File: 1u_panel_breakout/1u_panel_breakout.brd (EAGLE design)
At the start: 33 x 32 mm, 6 parts

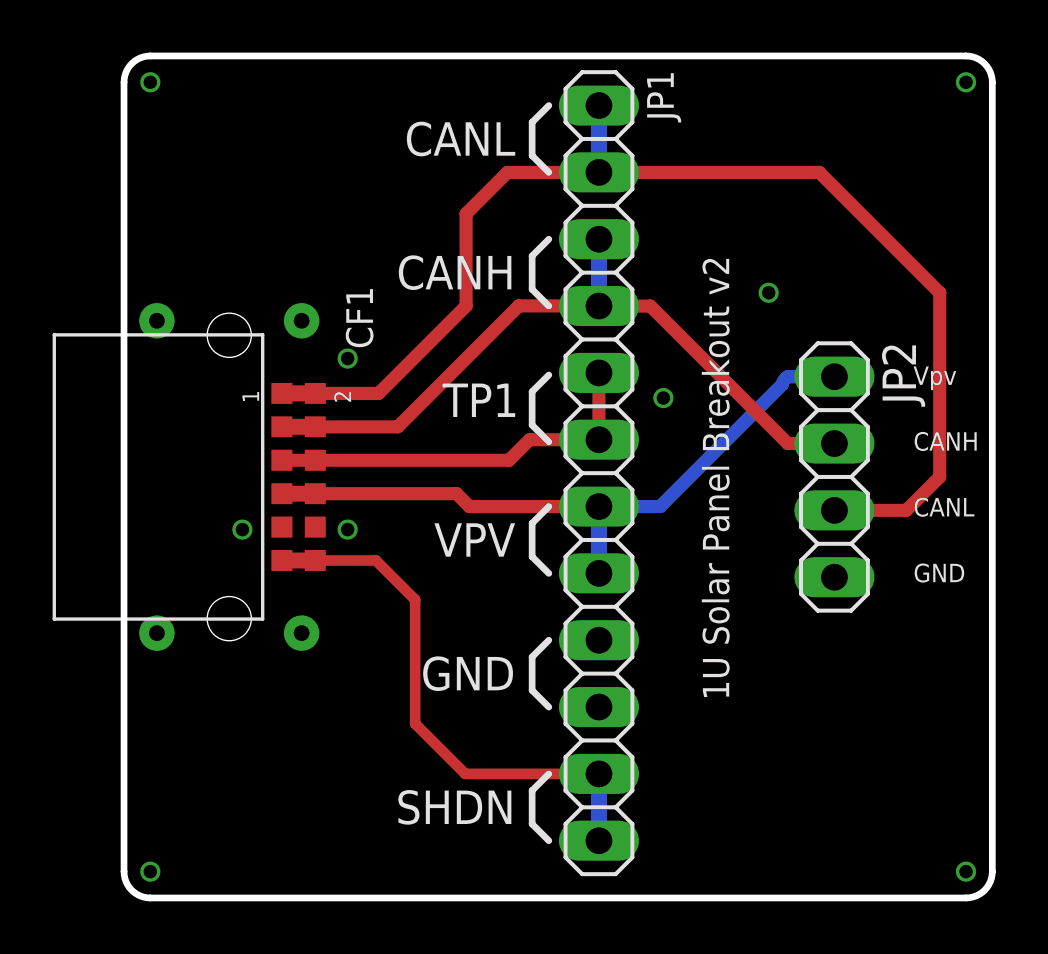
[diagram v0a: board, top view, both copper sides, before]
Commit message: Added part numbers to odd connectors.
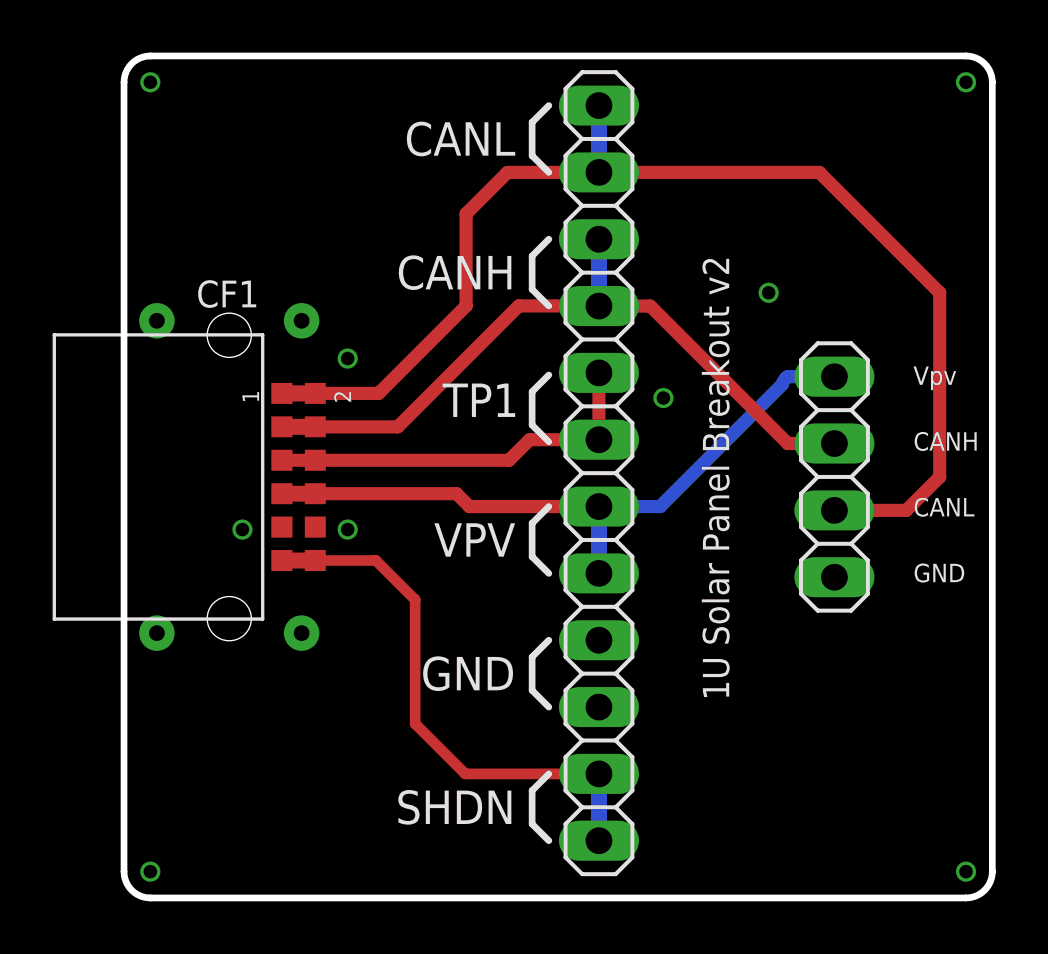
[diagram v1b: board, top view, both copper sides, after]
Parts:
- CF1: value ORESAT-SOLARPANEL-CARD-12PIN -> 15150122401000
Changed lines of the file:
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@@
 <layer number="14" name="Route14" color="1" fill="6" visible="no" active="no"/>
 <layer number="15" name="Route15" color="4" fill="6" visible="no" active="no"/>
-<layer number="16" name="Bottom" color="1" fill="1" visible="yes" active="yes"/>
+<layer number="16" name="Bottom" color="1" fill="1" visible="no" active="yes"/>
 <layer number="17" name="Pads" color="2" fill="1" visible="yes" active="yes"/>
 <layer number="18" name="Vias" color="2" fill="1" visible="yes" active="yes"/>
@@
 <layer number="20" name="Dimension" color="15" fill="1" visible="yes" active="yes"/>
 <layer number="21" name="tPlace" color="7" fill="1" visible="yes" active="yes"/>
-<layer number="22" name="bPlace" color="7" fill="1" visible="yes" active="yes"/>
+<layer number="22" name="bPlace" color="7" fill="1" visible="no" active="yes"/>
 <layer number="23" name="tOrigins" color="15" fill="1" visible="yes" active="yes"/>
-<layer number="24" name="bOrigins" color="15" fill="1" visible="yes" active="yes"/>
-<layer number="25" name="tNames" color="7" fill="1" visible="no" active="yes"/>
+<layer number="24" name="bOrigins" color="15" fill="1" visible="no" active="yes"/>
+<layer number="25" name="tNames" color="7" fill="1" visible="yes" active="yes"/>
 <layer number="26" name="bNames" color="7" fill="1" visible="no" active="yes"/>
 <layer number="27" name="tValues" color="7" fill="1" visible="no" active="yes"/>
 <layer number="28" name="bValues" color="7" fill="1" visible="no" active="yes"/>
 <layer number="29" name="tStop" color="7" fill="3" visible="yes" active="yes"/>
-<layer number="30" name="bStop" color="7" fill="6" visible="yes" active="yes"/>
+<layer number="30" name="bStop" color="7" fill="6" visible="no" active="yes"/>
 <layer number="31" name="tCream" color="7" fill="4" visible="no" active="yes"/>
 <layer number="32" name="bCream" color="7" fill="5" visible="no" active="yes"/>
@@
 <layer number="46" name="Milling" color="3" fill="1" visible="yes" active="yes"/>
 <layer number="47" name="Measures" color="7" fill="1" visible="no" active="yes"/>
-<layer number="48" name="Document" color="7" fill="1" visible="yes" active="yes"/>
-<layer number="49" name="Reference" color="7" fill="1" visible="yes" active="yes"/>
+<layer number="48" name="Document" color="7" fill="1" visible="no" active="yes"/>
+<layer number="49" name="Reference" color="7" fill="1" visible="no" active="yes"/>
 <layer number="50" name="dxf" color="7" fill="1" visible="no" active="no"/>
-<layer number="51" name="tDocu" color="7" fill="1" visible="yes" active="yes"/>
-<layer number="52" name="bDocu" color="7" fill="1" visible="yes" active="yes"/>
+<layer number="51" name="tDocu" color="7" fill="1" visible="no" active="yes"/>
+<layer number="52" name="bDocu" color="7" fill="1" visible="no" active="yes"/>
 <layer number="53" name="tGND_GNDA" color="7" fill="9" visible="no" active="no"/>
 <layer number="54" name="bGND_GNDA" color="1" fill="9" visible="no" active="no"/>
@@
 </autorouter>
 <elements>
-<element name="CF1" library="oresat-connectors" package="CON-1.27-M-RA-HARTING-1515012X401XXX" value="ORESAT-SOLARPANEL-CARD-12PIN" x="4" y="16" smashed="yes" rot="R270">
-<attribute name="NAME" x="8.445" y="23.255" size="1.016" layer="25" ratio="20" rot="R270"/>
+<element name="CF1" library="oresat-connectors" package="CON-1.27-M-RA-HARTING-1515012X401XXX" value="15150122401000" x="4" y="16" smashed="yes" rot="R270">
+<attribute name="NAME" x="2.745" y="22.445" size="1.016" layer="25" ratio="20"/>
 <attribute name="VALUE" x="-0.445" y="22.62" size="0.635" layer="27" ratio="20" rot="R270"/>
 </element>
 <element name="JP1" library="pinhead" package="1X12" value="" x="18.05" y="16.145" smashed="yes" rot="R270">
-<attribute name="NAME" x="19.8788" y="31.4612" size="1.016" layer="25" ratio="10" rot="R270"/>
 <attribute name="VALUE" x="14.875" y="31.385" size="1.27" layer="27" rot="R270"/>
 </element>
-<element name="JP2" library="pinhead" library_urn="urn:adsk.eagle:library:325" package="1X04" package3d_urn="urn:adsk.eagle:package:22407/2" value="" x="27" y="16" rot="R270"/>
+<element name="JP2" library="pinhead" library_urn="urn:adsk.eagle:library:325" package="1X04" package3d_urn="urn:adsk.eagle:package:22407/2" value="" x="27" y="16" smashed="yes" rot="R270">
+<attribute name="VALUE" x="23.825" y="21.08" size="1.27" layer="27" rot="R270"/>
+</element>
 <element name="U$1" library="oresat-misc" package="SCOPE_CLIP" value="SCOPE_CLIP" x="22.5" y="2" rot="R270"/>
 <element name="U$2" library="oresat-misc" package="SCOPE_CLIP" value="SCOPE_CLIP" x="22" y="30" rot="R90"/>

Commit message: Updated solar breakout board (for main connector).
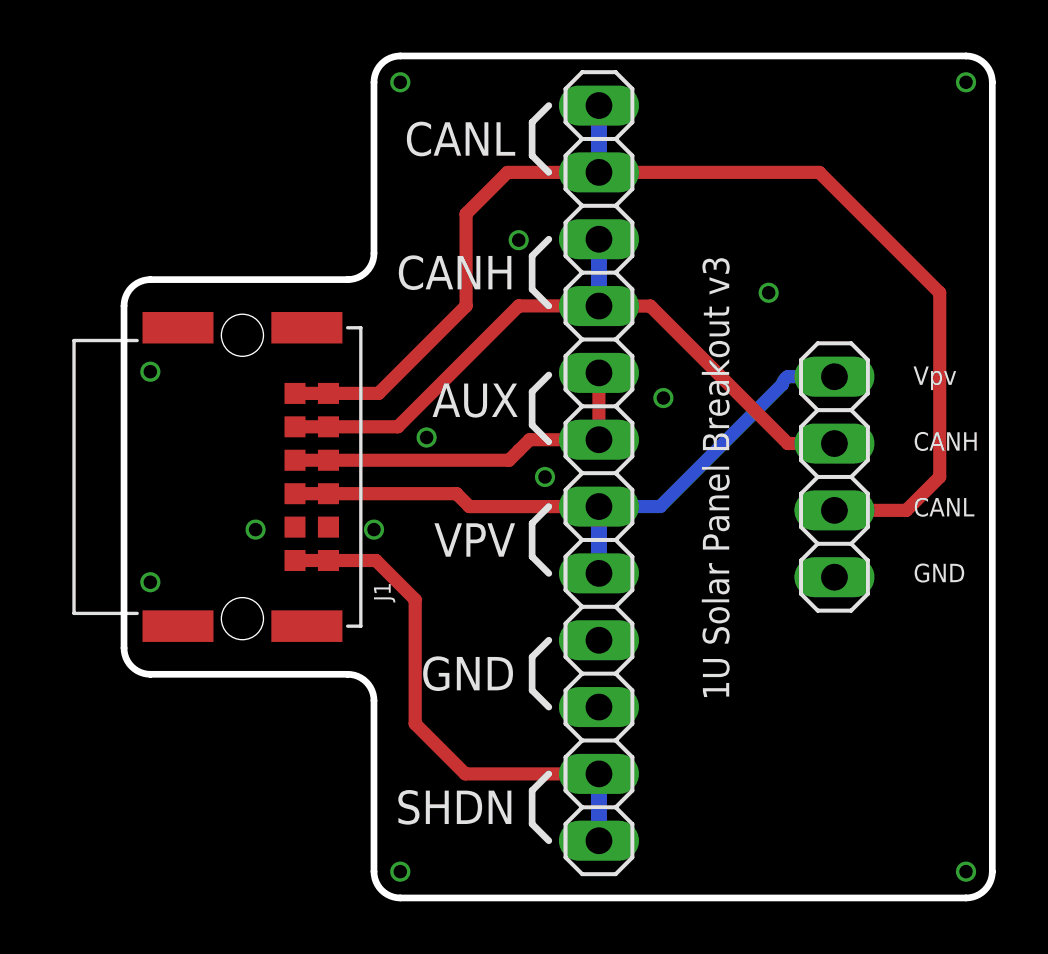
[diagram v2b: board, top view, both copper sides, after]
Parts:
- removed CF1: 15150122401000, oresat-connectors:CON-1.27-M-RA-HARTING-1515012X401XXX
- added J1: M55-7101242R, J-Harwin-M55-7101242-12pin-1.27mm-M-RA:M55-7101242R
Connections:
- net CANH: now also J1.10, J1.9; no longer CF1.3, CF1.4
- net CANL: now also J1.11, J1.12; no longer CF1.1, CF1.2
- net GND: now also J1.3, J1.4, J1.P$1, J1.P$2, J1.P$3, J1.P$4; no longer CF1.10, CF1.9
- net ORESAT-SHDN: now also J1.1, J1.2; no longer CF1.11, CF1.12
- net TP1: now also J1.7, J1.8; no longer CF1.5, CF1.6
- net VPV: now also J1.5, J1.6; no longer CF1.7, CF1.8
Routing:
- net VPV: track 25.8 -> 25.3 mm
- net CANH: track 27.6 -> 27.1 mm
- net TP1: track 14.9 -> 14.4 mm
- net ORESAT-SHDN: track 20.7 -> 20.2 mm
- net CANL: track 46.5 -> 46.0 mm
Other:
- outline, holes or cut-outs redrawn
- board text added: "1U Solar Panel Breakout v3"
- board text added: "AUX"
- board text removed: "1U Solar Panel Breakout v2"
- board text removed: "TP1"
